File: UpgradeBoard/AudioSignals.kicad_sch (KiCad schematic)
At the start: 19 parts, among them J1 Conn_02x05_Counter_Clockwise

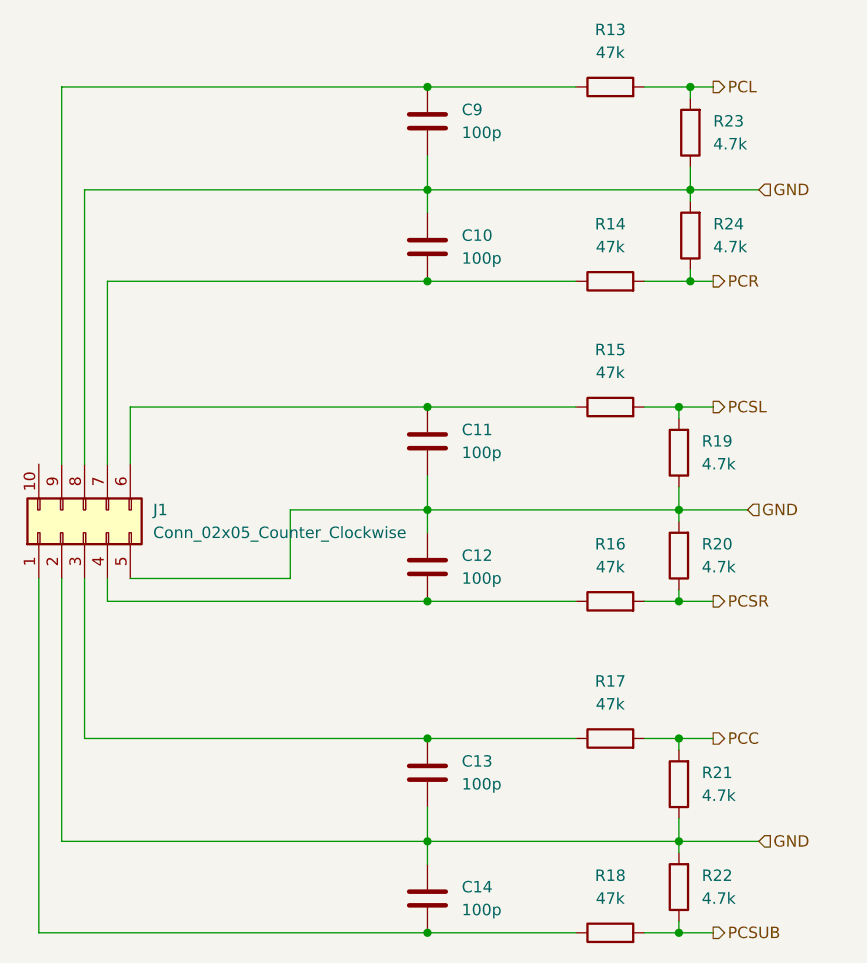
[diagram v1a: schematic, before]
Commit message: friday update
new hierarchical sheets, cabling, switching for main demux
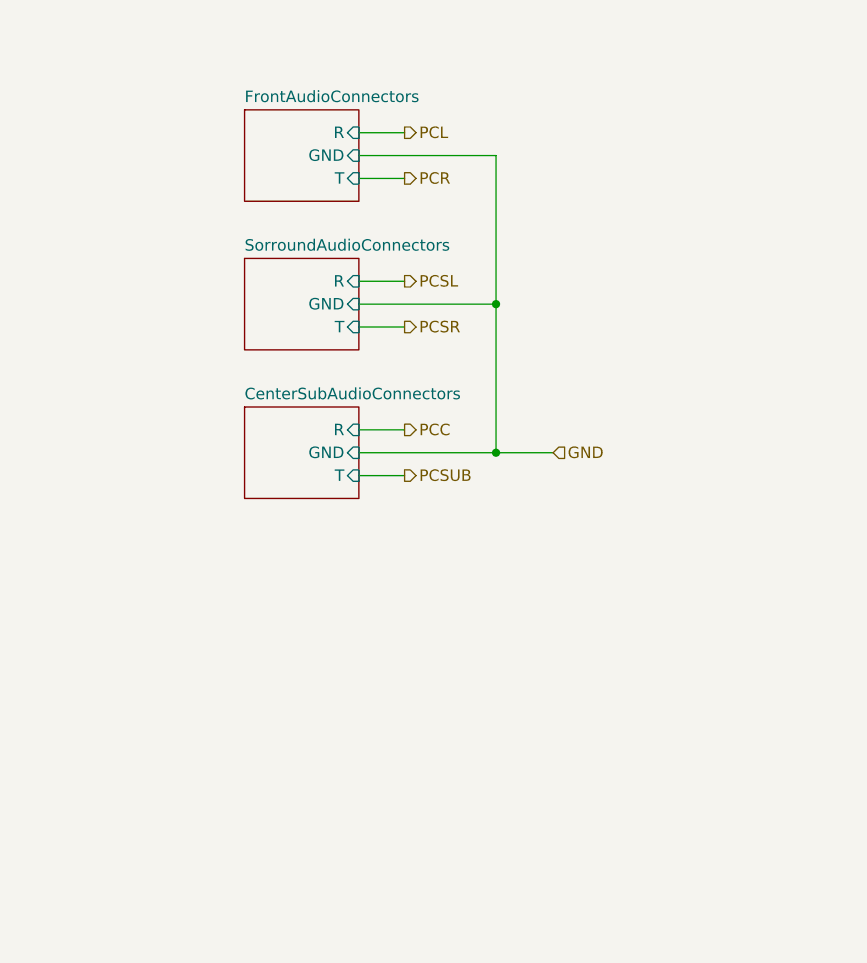
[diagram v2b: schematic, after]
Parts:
- removed C10, C11, C12, C13, C14, C9: 100p, symbol Device:C
- removed J1: Conn_02x05_Counter_Clockwise, symbol Connector_Generic:Conn_02x05_Counter_Clockwise
- removed R13, R14, R15, R16, R17, R18: 47k, symbol Device:R
- removed R19, R20, R21, R22, R23, R24: 4.7k, symbol Device:R
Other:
- added sheet CenterSubAudioConnectors (AudioConnectors.kicad_sch)
- added sheet FrontAudioConnectors (AudioConnectors.kicad_sch)
- added sheet SorroundAudioConnectors (AudioConnectors.kicad_sch)

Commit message: psucorrection
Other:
- added sheet CenterSubOpAmp (OpAmp.kicad_sch)
- added sheet FrontOpAmp (OpAmp.kicad_sch)
- added sheet SurroundOpAmp (OpAmp.kicad_sch)
